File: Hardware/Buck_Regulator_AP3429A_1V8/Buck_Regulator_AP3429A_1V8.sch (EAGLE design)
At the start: 30 parts, among them J1 Screw Terminal, J2 POWER_JACKPOWER_JACK_SLOT_COM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, J3 Breakout Headers, U1 AP3429/A

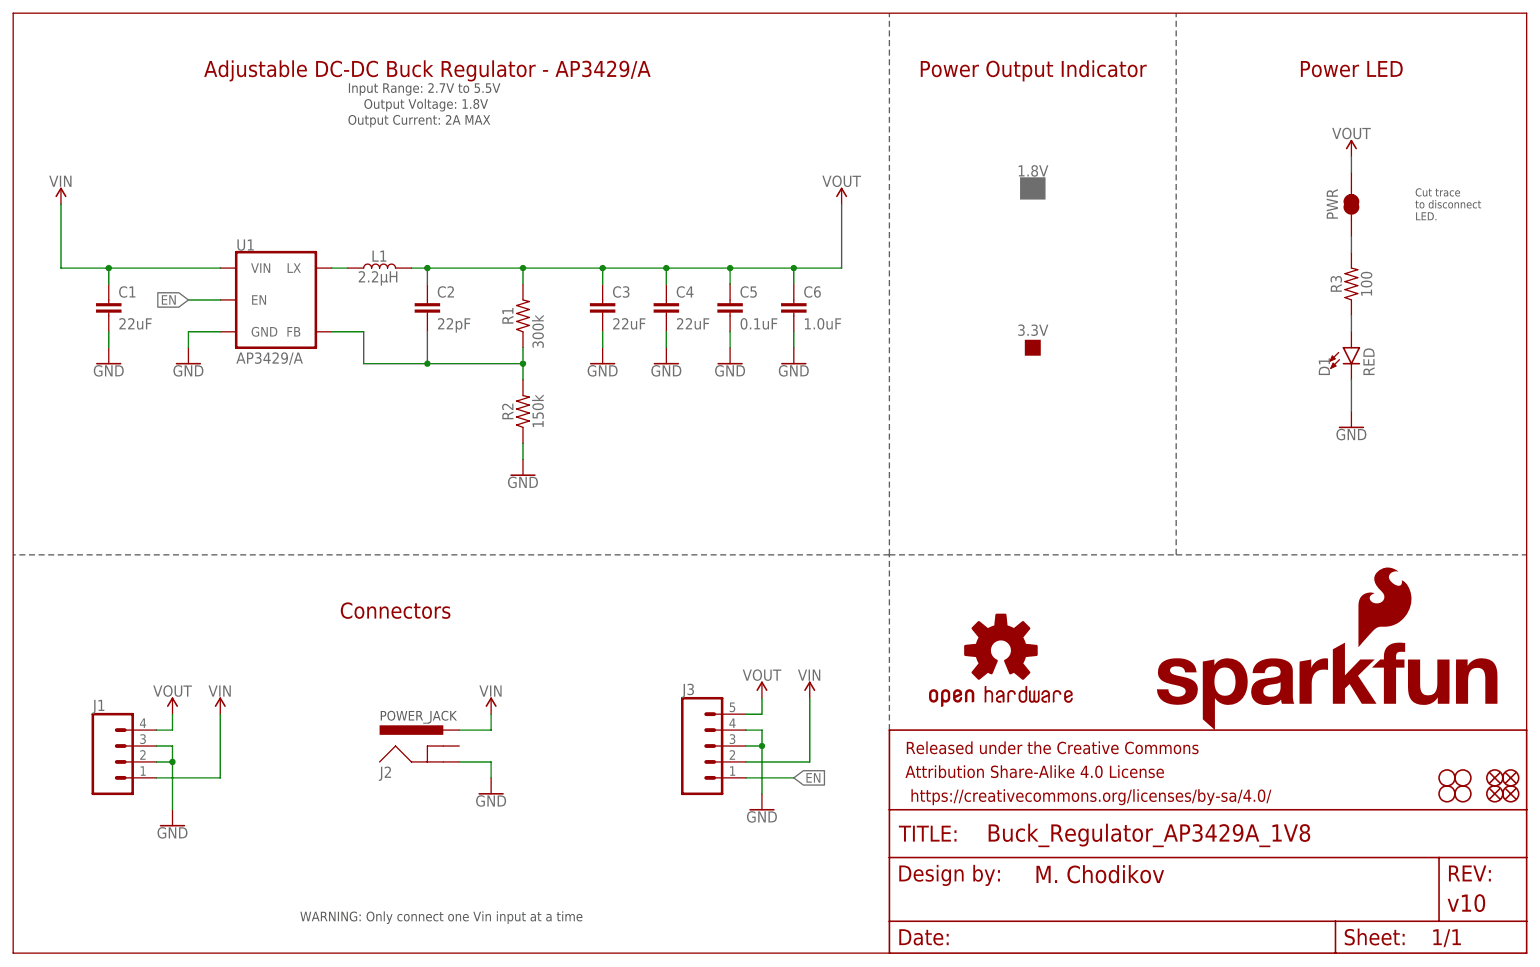
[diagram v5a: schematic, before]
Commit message: V11 Design Update
Added 100k resistor to pull EN high to VIN for an easier plug and play application.
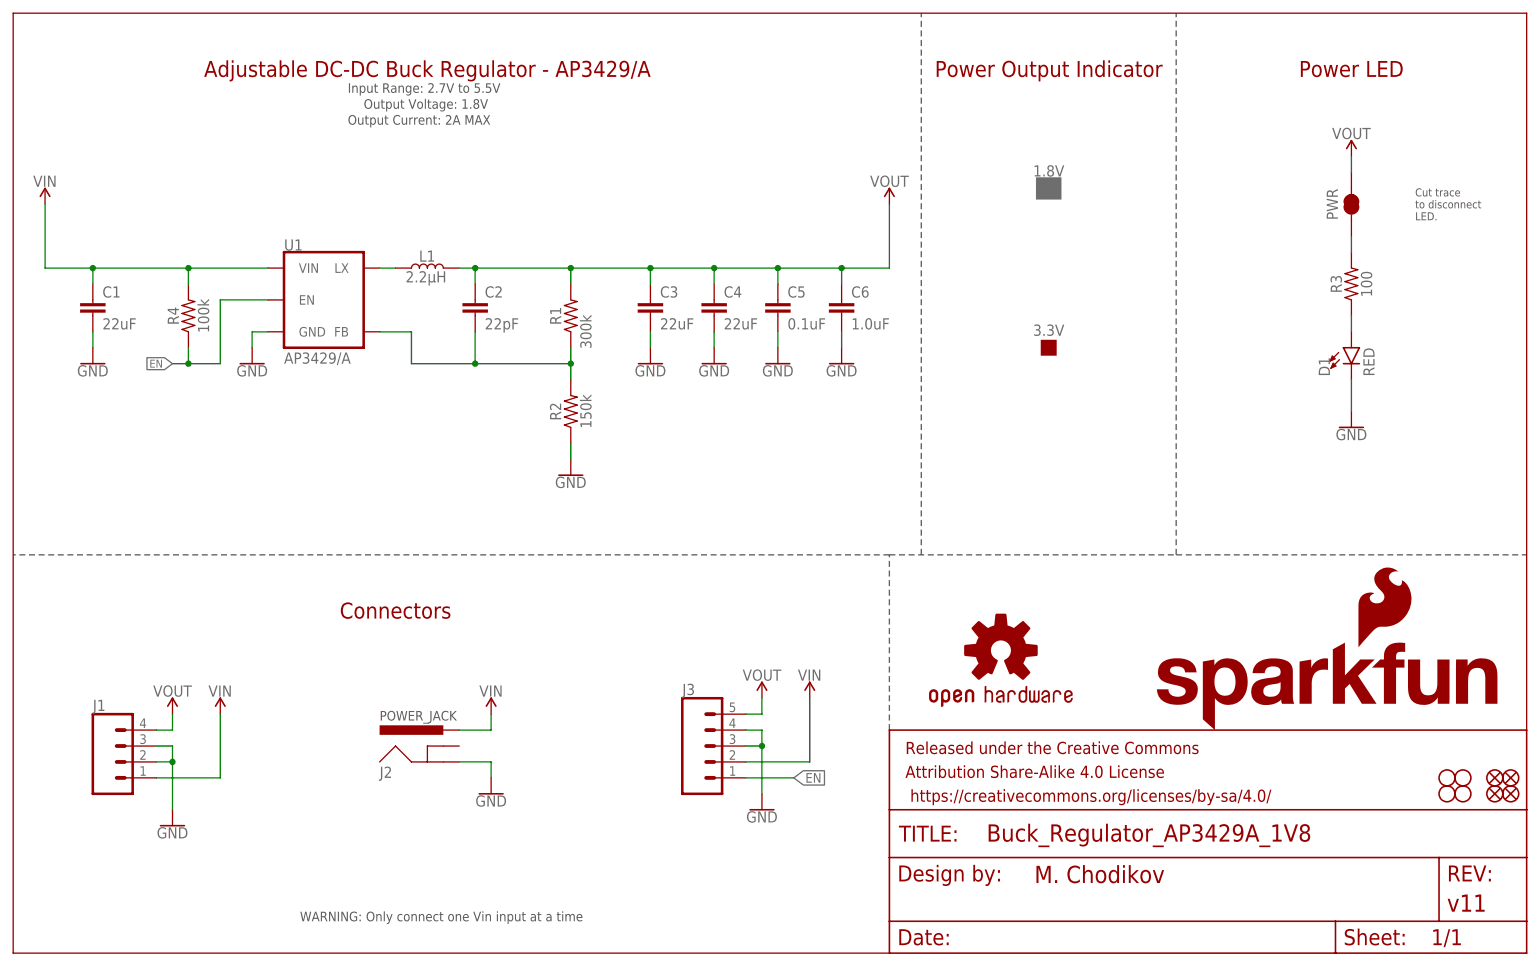
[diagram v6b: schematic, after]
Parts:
- added R4: 100k, SparkFun-Resistors:100KOHM-0603-1/10W-1%
- FRAME1: REV v10 -> v11
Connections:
- net EN: now also R4.1
- net VIN: now also R4.2
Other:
- moved on the sheet: 1.8V, 3.3V, C1, C2, C3, C4, C5, C6, L1, R1, R2, U1
